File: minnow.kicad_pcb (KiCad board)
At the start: 2 copper layers, 40 x 33 mm, 69 parts, among them J1 USB_C_Receptacle_Host, J2 USB_C_Receptacle_Dev, J3 ARM_JTAG_SWD_10_Male, J4 VCCIO_EXT, J5 PicoBlade, SW1 SW_DIP_x04, U1 FT230XQ, U2 PI5A3157CEX, U3 PI5A3157CEX, U4 USB3740B-AI2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

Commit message: README started
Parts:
- J3: footprint AkiyukiOkayasu/Kicad_Akiyuki_Footprint.pretty:SWD_2x05_P1.27mm_Vertical_SMD -> tuna-f1sh/jbr-kicad/Misc.pretty:20021521-00010T1LF
- R10: value 680R -> 22k
- R11: value 680R -> 10k
- R15, R7, R8, R9: value 1k -> 680R
- moved J3 0.88 mm to (172.3, 59.7), turned to 0 degrees
- moved G*** 0.25 mm to (168.0, 68.0)
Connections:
- net /SWDCLK renamed /SWCLK
- net /SWDO renamed /SWO
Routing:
- net GND: track 67.4 -> 55.8 mm
- net /VREF: track 15.2 -> 20.0 mm, vias 1 -> 2
- net /SWO: track 30.8 -> 28.2 mm
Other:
- board text added: "SWCLK"
- board text added: "SWO"
- board text removed: "CERN OHL 2"
- board text removed: "SWDCLK"
- board text removed: "SWDO"

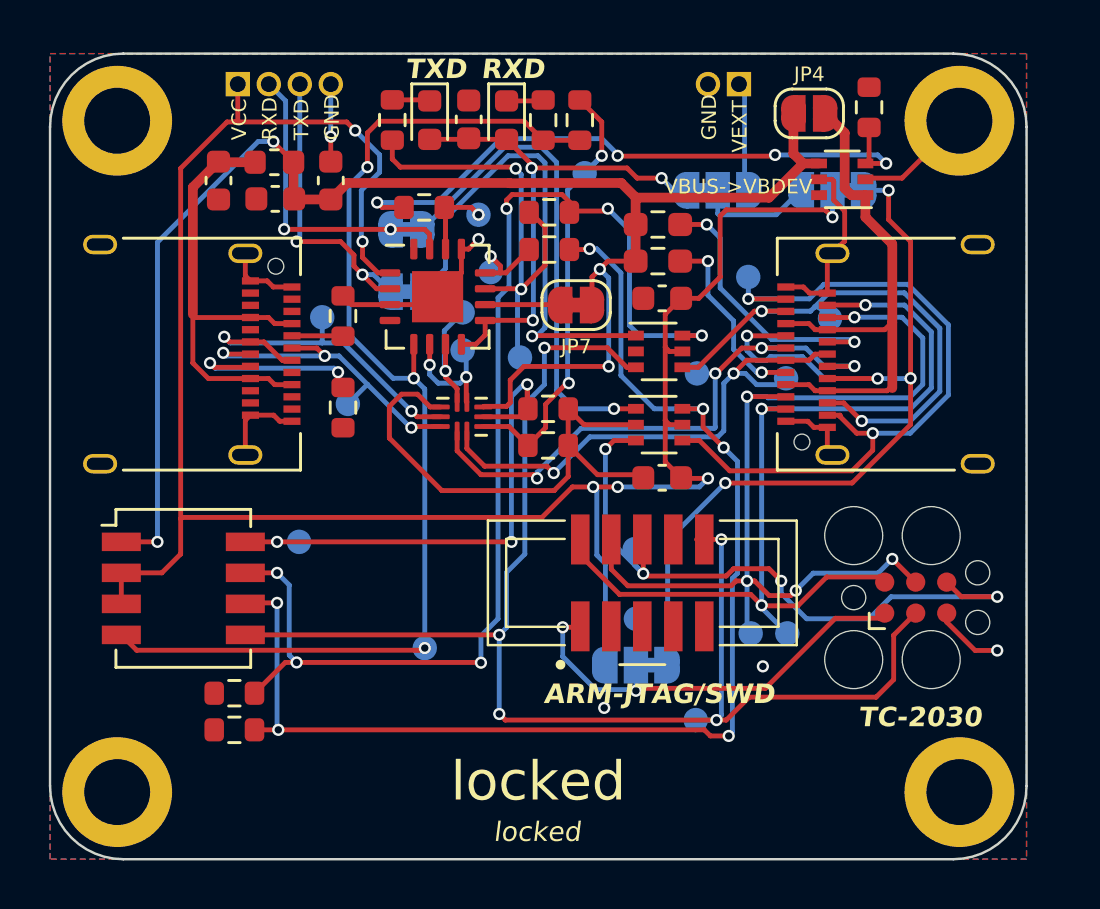
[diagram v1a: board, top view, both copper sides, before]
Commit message: plug not receptacle for device (TS)
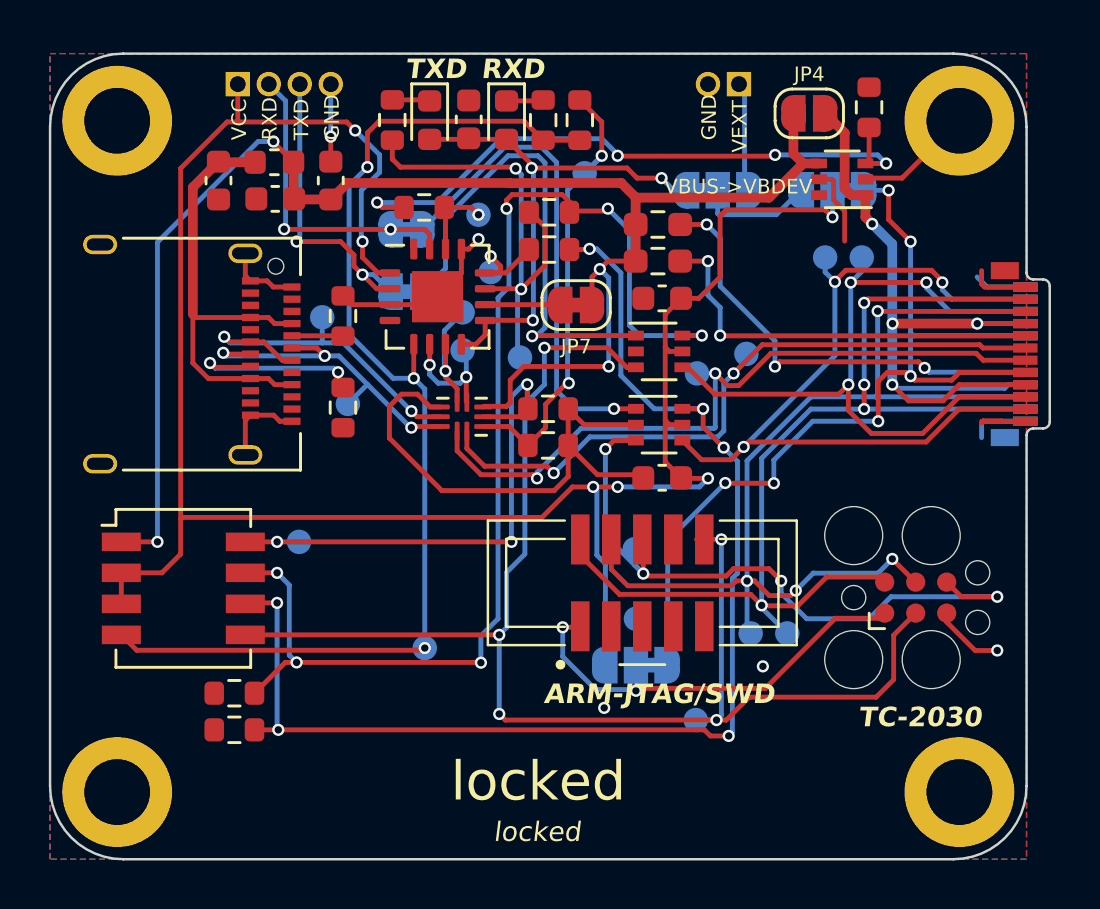
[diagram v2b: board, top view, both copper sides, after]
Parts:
- removed J2: USB_C_Receptacle_Dev, Connector_USB:USB_C_Receptacle_Amphenol_12401610E4-2A
- added P1: USB_C_Plug, Connector_USB:USB_C_Plug_Molex_105444, F.Cu at (188.0, 50.3)
- moved TP17 3.25 mm to (179.8, 46.4)
- moved TP18 2.82 mm to (181.2, 46.4)
- moved TP15 1.91 mm to (176.5, 50.3)
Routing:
- net /VBUS_DEV: track 21.8 -> 31.6 mm, vias 0 -> 4
- net /DEV_CC1: track 7.72 -> 16.9 mm
- net /DEV_RX-: track 22.2 -> 29.8 mm, vias 2 -> 3
- net /DEV_CC2: track 11.4 -> 18.6 mm, vias 2 -> 3
- net /DEV_D+: track 21.1 -> 28.1 mm
- net /DEV_D-: track 24.3 -> 29.4 mm, vias 4 -> 2
- net /SWDIO: track 39.3 -> 44.0 mm, vias 3 -> 4
- net /SWCLK: track 40.3 -> 44.3 mm, vias 5 -> 4
- net /DEV_RX+: track 29.7 -> 33.4 mm, vias 2 -> 3
- net GND: track 55.8 -> 58.8 mm
- net /VTARGET: track 39.5 -> 38.1 mm, vias 5 -> 6
- net Net-(J4-Pin_1): track 4.53 -> 3.92 mm
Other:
- board size 40 x 33 mm -> 41 x 33 mm
